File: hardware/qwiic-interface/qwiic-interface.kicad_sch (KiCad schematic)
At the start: 18 parts

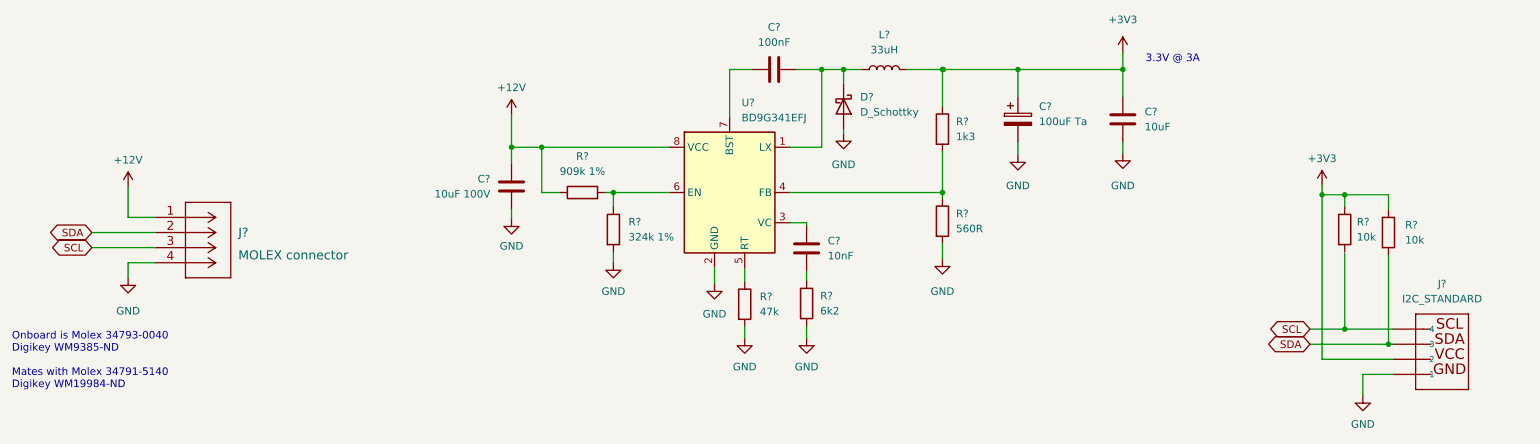
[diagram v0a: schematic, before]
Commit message: v1.0 of qwiic interface board layout
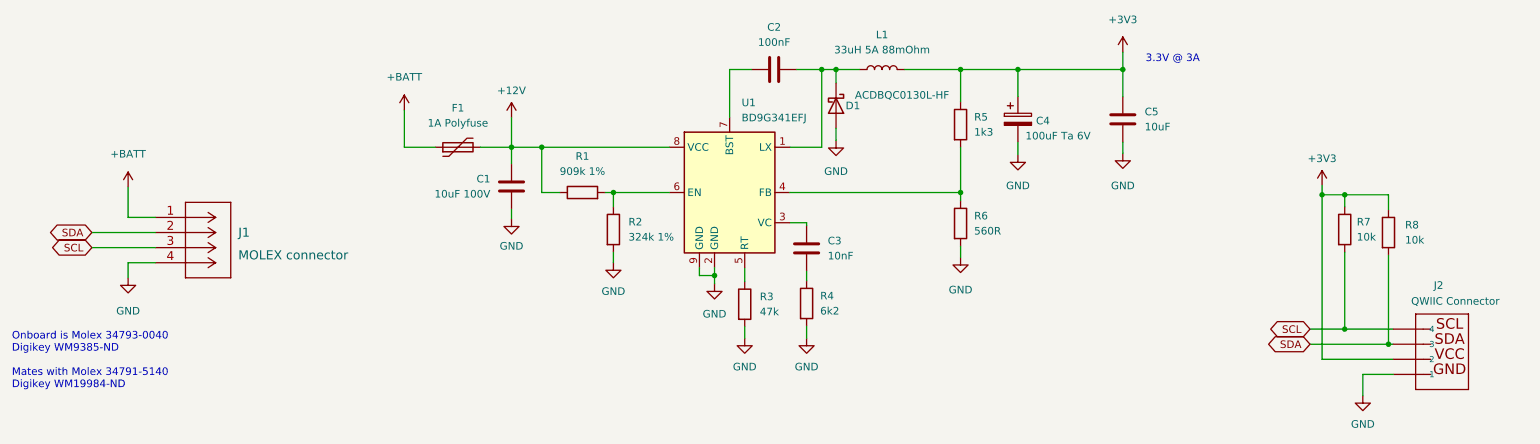
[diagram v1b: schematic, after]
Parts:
- removed C?: 100uF Ta, symbol Device:C_Polarized
- removed D?: D_Schottky, symbol Device:D_Schottky
- removed L?: 33uH, symbol Device:L
- removed U?: BD9G341EFJ, Package_SO:HTSOP-8-1EP_3.9x4.9mm_P1.27mm_EP2.4x3.2mm_ThermalVias, symbol Regulator_Switching:BD9G341EFJ
- added C4: 100uF Ta 6V, Capacitor_Tantalum_SMD:CP_EIA-3216-10_Kemet-I_Pad1.58x1.35mm_HandSolder, symbol Device:C_Polarized
- added D1: ACDBQC0130L-HF, Diode_SMD:D_SOD-923, symbol Device:D_Schottky
- added F1: 1A Polyfuse, Resistor_SMD:R_0805_2012Metric_Pad1.20x1.40mm_HandSolder, symbol Device:Polyfuse
- added L1: 33uH 5A 88mOhm, Beirdo:PM4346.333NLT, symbol Device:L
- added U1: BD9G341EFJ, Package_SO:HTSOP-8-1EP_3.9x4.9mm_P1.27mm_EP2.4x3.2mm_ThermalVias, symbol Beirdo:BD9G341EFJ
- C1: renamed from C?; footprint (none) -> Capacitor_SMD:C_1210_3225Metric_Pad1.33x2.70mm_HandSolder
- C2, C3, C5: renamed from C?; footprint (none) -> Capacitor_SMD:C_0805_2012Metric_Pad1.18x1.45mm_HandSolder
- J2: renamed from J?; value I2C_STANDARD -> QWIIC Connector; footprint UltraLibrarian:PRT-16766 -> Beirdo:QWIIC Connector
- R1, R2, R3, R4, R5, R6, R7, R8: renamed from R?; footprint (none) -> Resistor_SMD:R_0805_2012Metric_Pad1.20x1.40mm_HandSolder
- gave numbers to parts that had none: 1
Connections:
- net +12V: now also F1.2, U1.8 (VCC); no longer J1.1
- net +3V3: now also R5.1, C4.1, L1.2
- net GND: now also C4.2, D1.2 (A), U1.2 (GND), U1.9 (GND)
- net SCL: now also R7.2
- net at C2.2: now also D1.1 (K), L1.1, U1.1 (LX)
- net at C3.1: now also U1.3 (VC)
- net at R5.2, R6.1: now also U1.4 (FB)
- net at R3.1: now also U1.5 (RT)
- net at R1.2, R2.1: now also U1.6 (EN)
- net at C2.1: now also U1.7 (BST)
- new net +BATT: F1.1, J1.1
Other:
- moved on the sheet: R5, R6

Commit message: Update title block for qwiic-interface, add PDFs
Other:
- company: (none) -> Gavin Hurlbut
- title: (none) -> QWIIC Interface Board
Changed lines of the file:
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@@
 (kicad_sch (version 20211123) (generator eeschema)
   (paper "A4")
+  (title_block
+    (title "QWIIC Interface Board")
+    (date "2023-01-31")
+    (rev "1.0")
+    (company "Gavin Hurlbut")
+  )
   (junction (at 113.03 85.471) (diameter 0) (color 0 0 0 0)
   )

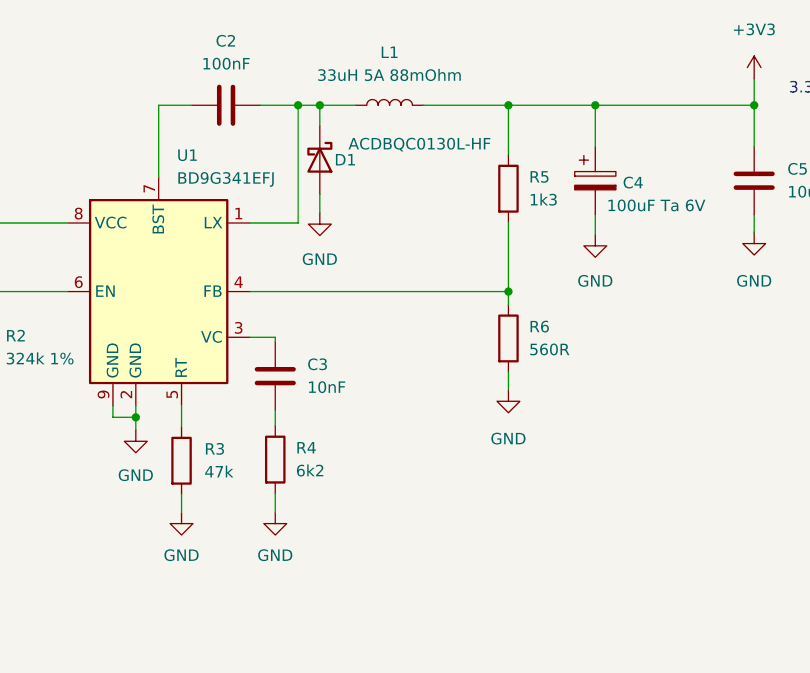
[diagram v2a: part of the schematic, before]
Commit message: Got rid of TINY diode (0402!?!?), remove USE_USB, put in PicoW
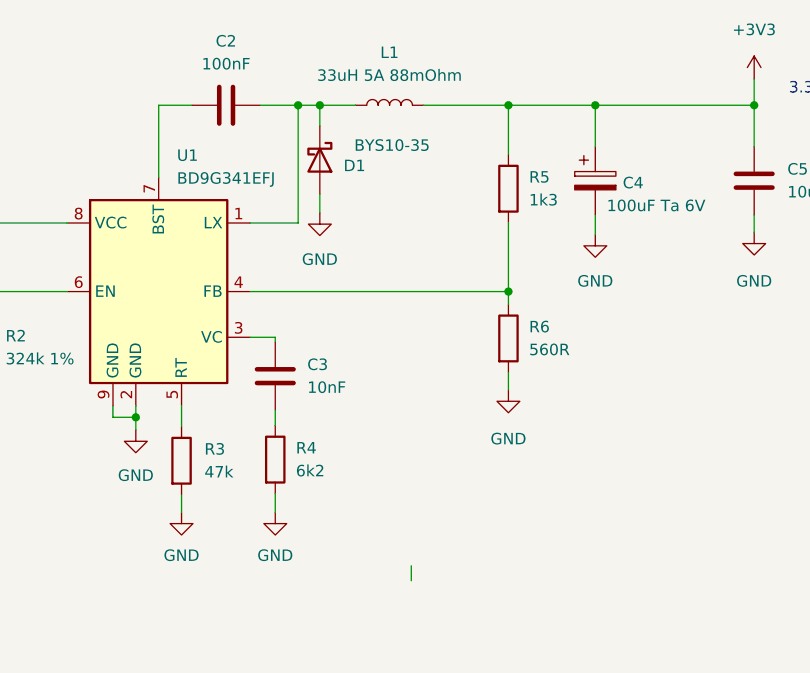
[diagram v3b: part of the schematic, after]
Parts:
- D1: value ACDBQC0130L-HF -> BYS10-35; footprint Diode_SMD:D_SOD-923 -> Diode_SMD:D_SMA_Handsoldering
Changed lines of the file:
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@@
   (title_block
     (title "QWIIC Interface Board")
-    (date "2023-01-31")
-    (rev "1.0")
+    (date "2023-02-14")
+    (rev "2.0")
     (company "Gavin Hurlbut")
   )
@@
   )
   (wire (pts (xy 248.158 103.124) (xy 248.158 116.078))
+    (stroke (width 0) (type default) (color 0 0 0 0))
+  )
+  (wire (pts (xy 172.72 125.222) (xy 172.72 123.571))
     (stroke (width 0) (type default) (color 0 0 0 0))
   )
@@
     )
     (pin "1")
+  )
+  (symbol (lib_id "Device:D_Schottky") (at 162.56 78.486 270) (unit 1)
+    (in_bom yes) (on_board yes)
+    (property "Reference" "D1" (id 0) (at 167.64 79.121 90)
+      (effects (font (size 1.27 1.27)) (justify right))
+    )
+    (property "Value" "BYS10-35" (id 1) (at 174.8028 76.8604 90)
+      (effects (font (size 1.27 1.27)) (justify right))
+    )
+    (property "Footprint" "Diode_SMD:D_SMA_Handsoldering" (id 2) (at 162.56 78.486 0)
+      (effects (font (size 1.27 1.27)) hide)
+    )
+    (property "Datasheet" "~" (id 3) (at 162.56 78.486 0)
+      (effects (font (size 1.27 1.27)) hide)
+    )
+    (pin "1")
+    (pin "2")
   )
   (symbol (lib_id "Beirdo:BD9G341EFJ") (at 144.653 93.091 0) (unit 1)
@@
     (pin "2")
   )
-  (symbol (lib_id "Device:D_Schottky") (at 162.56 78.486 270) (unit 1)
-    (in_bom yes) (on_board yes)
-    (property "Reference" "D1" (id 0) (at 166.624 78.486 90)
-      (effects (font (size 1.27 1.27)) (justify right))
-    )
-    (property "Value" "ACDBQC0130L-HF" (id 1) (at 181.61 76.708 90)
-      (effects (font (size 1.27 1.27)) (justify right))
-    )
-    (property "Footprint" "Diode_SMD:D_SOD-923" (id 2) (at 162.56 78.486 0)
-      (effects (font (size 1.27 1.27)) hide)
-    )
-    (property "Datasheet" "~" (id 3) (at 162.56 78.486 0)
-      (effects (font (size 1.27 1.27)) hide)
-    )
-    (pin "1")
-    (pin "2")
-  )
   (symbol (lib_id "Device:Polyfuse") (at 98.933 85.471 90) (unit 1)
     (in_bom yes) (on_board yes) (fields_autoplaced)
@@
       (reference "C5") (unit 1) (value "10uF") (footprint "Capacitor_SMD:C_0805_2012Metric_Pad1.18x1.45mm_HandSolder")
     )
-    (path "/c6927288-5c3e-4c44-8f1e-b21d24c10732"
-      (reference "D1") (unit 1) (value "ACDBQC0130L-HF") (footprint "Diode_SMD:D_SOD-923")
+    (path "/72cc2226-f372-4055-abcf-65dfa2fd002c"
+      (reference "D1") (unit 1) (value "BYS10-35") (footprint "Diode_SMD:D_SMA_Handsoldering")
     )
     (path "/ce9f4ca6-358f-4ddd-bc7b-f3ab511b471a"
